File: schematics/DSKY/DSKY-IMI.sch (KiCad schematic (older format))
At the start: 4 parts, among them J103 Conn_02x08, J104 Conn_02x10, U5 74LS04, U6 74LS00

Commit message: Minor DSKY tweaks.
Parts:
- added U36: 74LS00, symbol 74xx:74LS00
- added U79: 74LS04, symbol 74xx:74LS04
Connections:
- net CLK2: now also U36.9
- net at J103.3 (Pin_3), U5.3: now also U79.5
- new net: U36.10, U79.6
- new net SGNRST: U36.8
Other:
- moved on the sheet: U5B, U6A
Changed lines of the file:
@@
 Comment4 ""
 $EndDescr
-Text HLabel 7450 2700 2    50   Output ~ 0
+Text HLabel 8500 2700 2    50   Output ~ 0
 CLK2
 Text HLabel 6250 2600 2    50   Output ~ 0
@@
 Text HLabel 5750 3300 0    50   Output ~ 0
 RPRO
-Text HLabel 8500 3050 2    50   Output ~ 0
+Text HLabel 8500 3200 2    50   Output ~ 0
 DSKYRST
 $Comp
 L 74xx:74LS00 U?
 U 1 1 6395652F
-P 8200 3050
+P 8200 3200
 AR Path="/5F5E4E3B/5F5F8347/6395652F" Ref="U?"  Part="1"
 AR Path="/60F98A72/6395652F" Ref="U?"  Part="1"
@@
 AR Path="/60F98A72/66CE2F9E/6395652F" Ref="U?"  Part="1"
 AR Path="/60F989FD/6395652F" Ref="U6"  Part="1"
-F 0 "U6" H 8200 3375 50  0000 C CNN
-F 1 "74LS00" H 8200 3284 50  0000 C CNN
-F 2 "" H 8200 3050 50  0001 C CNN
-F 3 "http://www.ti.com/lit/gpn/sn74ls00" H 8200 3050 50  0001 C CNN
-	1    8200 3050
+F 0 "U6" H 8200 3525 50  0000 C CNN
+F 1 "74LS00" H 8200 3434 50  0000 C CNN
+F 2 "" H 8200 3200 50  0001 C CNN
+F 3 "http://www.ti.com/lit/gpn/sn74ls00" H 8200 3200 50  0001 C CNN
+	1    8200 3200
 	1    0    0    -1
 $EndComp
@@
 L 74xx:74LS04 U?
 U 2 1 63956535
-P 7600 3150
+P 7250 3300
 AR Path="/5F5E4E3B/5F5F8347/63956535" Ref="U?"  Part="6"
 AR Path="/60F98A72/63956535" Ref="U?"  Part="2"
@@
 AR Path="/60F98A72/66CE2F9E/63956535" Ref="U?"  Part="6"
 AR Path="/60F989FD/63956535" Ref="U5"  Part="2"
-F 0 "U5" H 7700 2900 50  0000 C CNN
-F 1 "74LS04" H 7700 3000 50  0000 C CNN
-F 2 "" H 7600 3150 50  0001 C CNN
-F 3 "http://www.ti.com/lit/gpn/sn74LS04" H 7600 3150 50  0001 C CNN
-	2    7600 3150
-	1    0    0    -1
-$EndComp
-Wire Wire Line
-	6250 2800 7100 2800
-Wire Wire Line
-	7100 2800 7100 3150
-Wire Wire Line
-	7100 3150 7300 3150
-Wire Wire Line
-	6250 2700 7300 2700
-Wire Wire Line
-	7450 2700 7300 2700
-Wire Wire Line
-	7300 2950 7900 2950
+F 0 "U5" H 7300 3550 50  0000 C CNN
+F 1 "74LS04" H 7300 3450 50  0000 C CNN
+F 2 "" H 7250 3300 50  0001 C CNN
+F 3 "http://www.ti.com/lit/gpn/sn74LS04" H 7250 3300 50  0001 C CNN
+	2    7250 3300
+	1    0    0    -1
+$EndComp
+Wire Wire Line
+	6250 2800 6750 2800
+Wire Wire Line
+	6750 2800 6750 3300
+Wire Wire Line
+	6750 3300 6950 3300
+Wire Wire Line
+	8500 2700 7700 2700
+Wire Wire Line
+	7700 3100 7700 3650
 Text Notes 3350 4900 0    70   ~ 0
 Note: PROG, RPRO & PARALM are Active High,\nthe rest are Active Low with the clock signals\nand KB_STR being pulses.
 Wire Bus Line
 	2900 3550 4150 3550
-Connection ~ 7300 2700
 NoConn ~ 6250 3300
-Wire Wire Line
-	7300 2700 7300 2950
 NoConn ~ 5750 3100
-Wire Bus Line
-	4150 3000 4150 3550
-Wire Bus Line
-	2900 2200 2900 3550
 Text HLabel 5750 3200 0    50   Output ~ 0
 CLK3
+$Comp
+L 74xx:74LS00 U36
+U 3 1 6B3C3F3A
+P 8200 3750
+F 0 "U36" H 8200 4075 50  0000 C CNN
+F 1 "74LS00" H 8200 3984 50  0000 C CNN
+F 2 "" H 8200 3750 50  0001 C CNN
+F 3 "http://www.ti.com/lit/gpn/sn74ls00" H 8200 3750 50  0001 C CNN
+	3    8200 3750
+	1    0    0    -1
+$EndComp
+Text HLabel 8500 3750 2    50   Output ~ 0
+SGNRST
+$Comp
+L 74xx:74LS04 U79
+U 3 1 6B3C632F
+P 7250 3850
+F 0 "U79" H 7300 4100 50  0000 C CNN
+F 1 "74LS04" H 7300 4000 50  0000 C CNN
+F 2 "" H 7250 3850 50  0001 C CNN
+F 3 "http://www.ti.com/lit/gpn/sn74LS04" H 7250 3850 50  0001 C CNN
+	3    7250 3850
+	1    0    0    -1
+$EndComp
+Wire Wire Line
+	6750 3850 6950 3850
+Wire Wire Line
+	6750 3300 6750 3850
+Connection ~ 6750 3300
+Wire Wire Line
+	7550 3850 7900 3850
+Wire Wire Line
+	7550 3300 7900 3300
+Wire Wire Line
+	7900 3100 7700 3100
+Wire Wire Line
+	7700 3650 7900 3650
+Connection ~ 7700 2700
+Wire Wire Line
+	6250 2700 7700 2700
+Wire Wire Line
+	7700 2700 7700 3100
+Connection ~ 7700 3100
+Wire Bus Line
+	4150 3000 4150 3550
+Wire Bus Line
+	2900 2200 2900 3550
 $EndSCHEMATC

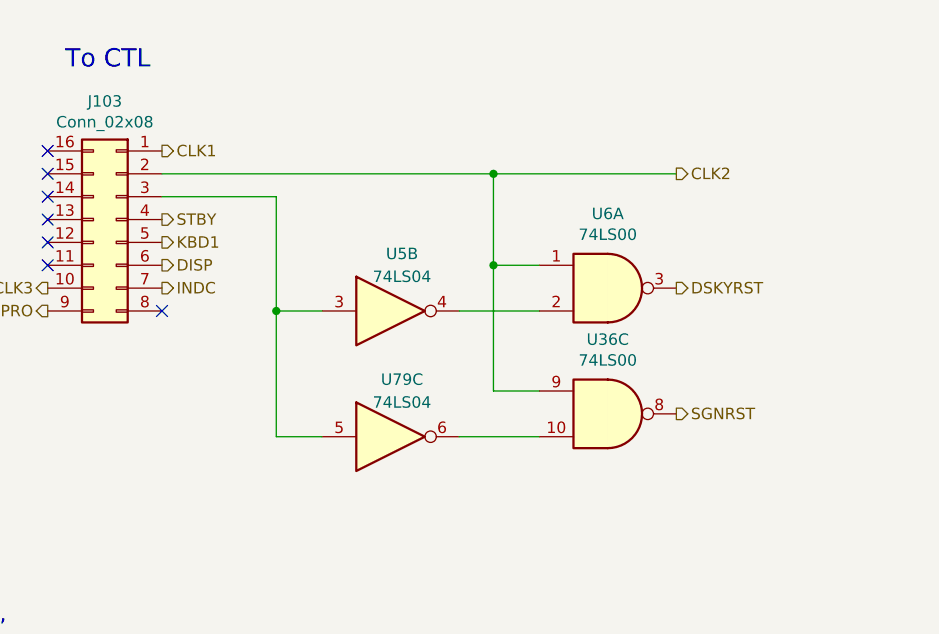
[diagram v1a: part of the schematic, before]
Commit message: Using 4 LED driver chips.
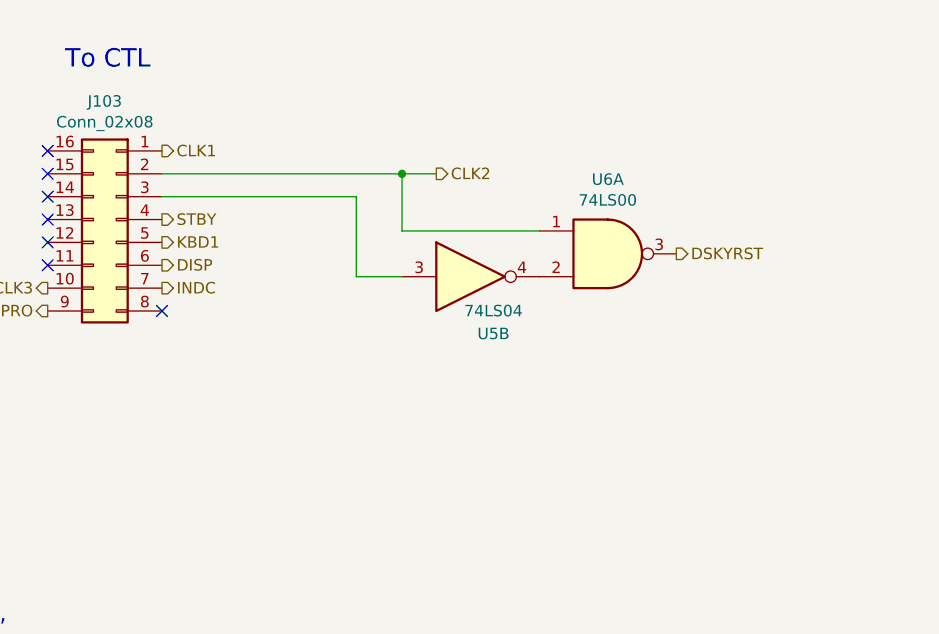
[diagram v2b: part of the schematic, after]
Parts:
- removed U36: 74LS00, symbol 74xx:74LS00
- removed U79: 74LS04, symbol 74xx:74LS04
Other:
- moved on the sheet: U5B, U6A
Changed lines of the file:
@@
 $Descr A 11000 8500
 encoding utf-8
-Sheet 2 15
+Sheet 12 13
 Title ""
 Date ""
@@
 Comment4 ""
 $EndDescr
-Text HLabel 8500 2700 2    50   Output ~ 0
+Text HLabel 7450 2700 2    50   Output ~ 0
 CLK2
 Text HLabel 6250 2600 2    50   Output ~ 0
@@
 $EndComp
 $Comp
-L power:GND #PWR0252
+L power:GND #PWR0196
 U 1 1 63206B7C
 P 9600 1000
-F 0 "#PWR0252" H 9600 750 50  0001 C CNN
+F 0 "#PWR0196" H 9600 750 50  0001 C CNN
 F 1 "GND" H 9605 827 50  0000 C CNN
 F 2 "" H 9600 1000 50  0001 C CNN
@@
 $EndComp
 $Comp
-L power:+5V #PWR0253
+L power:+5V #PWR0197
 U 1 1 6320B47A
 P 9100 1000
-F 0 "#PWR0253" H 9100 850 50  0001 C CNN
+F 0 "#PWR0197" H 9100 850 50  0001 C CNN
 F 1 "+5V" H 9115 1173 50  0000 C CNN
 F 2 "" H 9100 1000 50  0001 C CNN
@@
 Text HLabel 5750 3300 0    50   Output ~ 0
 RPRO
-Text HLabel 8500 3200 2    50   Output ~ 0
+Text HLabel 8500 3050 2    50   Output ~ 0
 DSKYRST
 $Comp
 L 74xx:74LS00 U?
 U 1 1 6395652F
-P 8200 3200
+P 8200 3050
 AR Path="/5F5E4E3B/5F5F8347/6395652F" Ref="U?"  Part="1"
 AR Path="/60F98A72/6395652F" Ref="U?"  Part="1"
@@
 AR Path="/60F98A72/66CE2F9E/6395652F" Ref="U?"  Part="1"
 AR Path="/60F989FD/6395652F" Ref="U6"  Part="1"
-F 0 "U6" H 8200 3525 50  0000 C CNN
-F 1 "74LS00" H 8200 3434 50  0000 C CNN
-F 2 "" H 8200 3200 50  0001 C CNN
-F 3 "http://www.ti.com/lit/gpn/sn74ls00" H 8200 3200 50  0001 C CNN
-	1    8200 3200
+F 0 "U6" H 8200 3375 50  0000 C CNN
+F 1 "74LS00" H 8200 3284 50  0000 C CNN
+F 2 "" H 8200 3050 50  0001 C CNN
+F 3 "http://www.ti.com/lit/gpn/sn74ls00" H 8200 3050 50  0001 C CNN
+	1    8200 3050
 	1    0    0    -1
 $EndComp
@@
 L 74xx:74LS04 U?
 U 2 1 63956535
-P 7250 3300
+P 7600 3150
 AR Path="/5F5E4E3B/5F5F8347/63956535" Ref="U?"  Part="6"
 AR Path="/60F98A72/63956535" Ref="U?"  Part="2"
@@
 AR Path="/60F98A72/66CE2F9E/63956535" Ref="U?"  Part="6"
 AR Path="/60F989FD/63956535" Ref="U5"  Part="2"
-F 0 "U5" H 7300 3550 50  0000 C CNN
-F 1 "74LS04" H 7300 3450 50  0000 C CNN
-F 2 "" H 7250 3300 50  0001 C CNN
-F 3 "http://www.ti.com/lit/gpn/sn74LS04" H 7250 3300 50  0001 C CNN
-	2    7250 3300
-	1    0    0    -1
-$EndComp
-Wire Wire Line
-	6250 2800 6750 2800
-Wire Wire Line
-	6750 2800 6750 3300
-Wire Wire Line
-	6750 3300 6950 3300
-Wire Wire Line
-	8500 2700 7700 2700
-Wire Wire Line
-	7700 3100 7700 3650
+F 0 "U5" H 7700 2900 50  0000 C CNN
+F 1 "74LS04" H 7700 3000 50  0000 C CNN
+F 2 "" H 7600 3150 50  0001 C CNN
+F 3 "http://www.ti.com/lit/gpn/sn74LS04" H 7600 3150 50  0001 C CNN
+	2    7600 3150
+	1    0    0    -1
+$EndComp
+Wire Wire Line
+	6250 2800 7100 2800
+Wire Wire Line
+	7100 2800 7100 3150
+Wire Wire Line
+	7100 3150 7300 3150
+Wire Wire Line
+	6250 2700 7300 2700
+Wire Wire Line
+	7450 2700 7300 2700
+Wire Wire Line
+	7300 2950 7900 2950
 Text Notes 3350 4900 0    70   ~ 0
 Note: PROG, RPRO & PARALM are Active High,\nthe rest are Active Low with the clock signals\nand KB_STR being pulses.
 Wire Bus Line
 	2900 3550 4150 3550
+Connection ~ 7300 2700
 NoConn ~ 6250 3300
-NoConn ~ 5750 3100
 Text HLabel 5750 3200 0    50   Output ~ 0
 CLK3
-$Comp
-L 74xx:74LS00 U36
-U 3 1 6B3C3F3A
-P 8200 3750
-F 0 "U36" H 8200 4075 50  0000 C CNN
-F 1 "74LS00" H 8200 3984 50  0000 C CNN
-F 2 "" H 8200 3750 50  0001 C CNN
-F 3 "http://www.ti.com/lit/gpn/sn74ls00" H 8200 3750 50  0001 C CNN
-	3    8200 3750
-	1    0    0    -1
-$EndComp
-Text HLabel 8500 3750 2    50   Output ~ 0
-SGNRST
-$Comp
-L 74xx:74LS04 U79
-U 3 1 6B3C632F
-P 7250 3850
-F 0 "U79" H 7300 4100 50  0000 C CNN
-F 1 "74LS04" H 7300 4000 50  0000 C CNN
-F 2 "" H 7250 3850 50  0001 C CNN
-F 3 "http://www.ti.com/lit/gpn/sn74LS04" H 7250 3850 50  0001 C CNN
-	3    7250 3850
-	1    0    0    -1
-$EndComp
-Wire Wire Line
-	6750 3850 6950 3850
-Wire Wire Line
-	6750 3300 6750 3850
-Connection ~ 6750 3300
-Wire Wire Line
-	7550 3850 7900 3850
-Wire Wire Line
-	7550 3300 7900 3300
-Wire Wire Line
-	7900 3100 7700 3100
-Wire Wire Line
-	7700 3650 7900 3650
-Connection ~ 7700 2700
-Wire Wire Line
-	6250 2700 7700 2700
-Wire Wire Line
-	7700 2700 7700 3100
-Connection ~ 7700 3100
+Wire Wire Line
+	7300 2700 7300 2950
+NoConn ~ 5750 3100
 Wire Bus Line
 	4150 3000 4150 3550

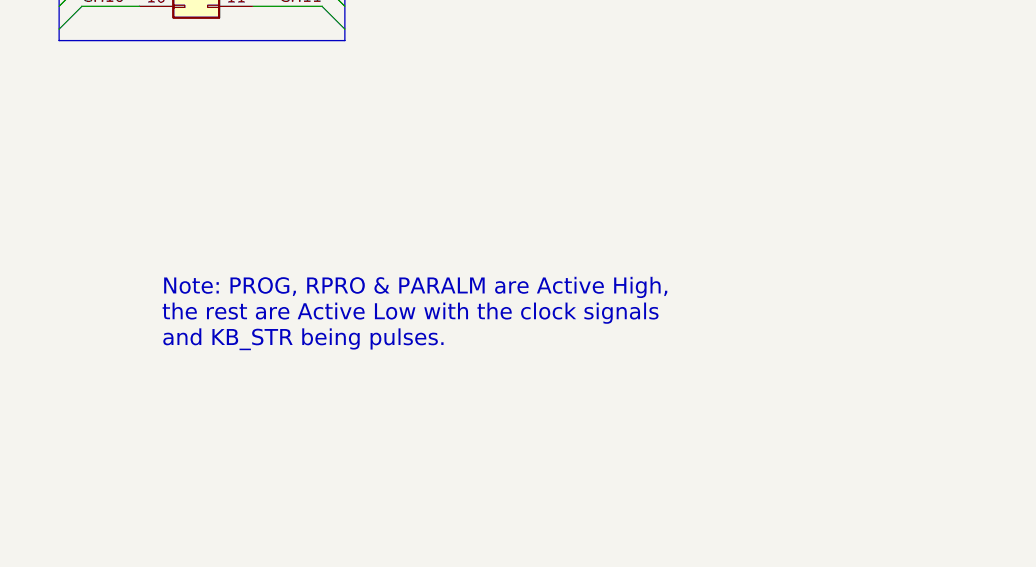
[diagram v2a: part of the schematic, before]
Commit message: Modified to use fourth display decoder chip.
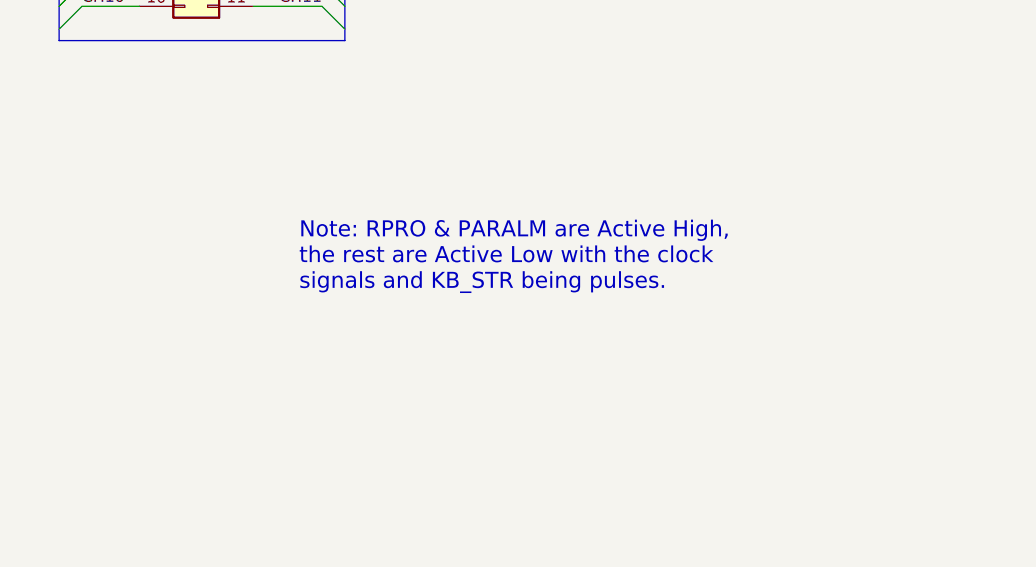
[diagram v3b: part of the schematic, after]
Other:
- note added: "Note: RPRO & PARALM are Active High,\nthe rest are Active Low with the clock \nsignals and KB_STR being pulses."
- note removed: "Note: PROG, RPRO & PARALM are Active High,\nthe rest are Active Low with the clock signals\nand KB_STR being pulses."
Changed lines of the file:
@@
 $Descr A 11000 8500
 encoding utf-8
-Sheet 12 13
+Sheet 12 14
 Title ""
 Date ""
@@
 Wire Wire Line
 	7300 2950 7900 2950
-Text Notes 3350 4900 0    70   ~ 0
-Note: PROG, RPRO & PARALM are Active High,\nthe rest are Active Low with the clock signals\nand KB_STR being pulses.
+Text Notes 3950 4650 0    70   ~ 0
+Note: RPRO & PARALM are Active High,\nthe rest are Active Low with the clock \nsignals and KB_STR being pulses.
 Wire Bus Line
 	2900 3550 4150 3550
